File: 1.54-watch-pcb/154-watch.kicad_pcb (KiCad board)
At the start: 4 copper layers, 50.3 x 33 mm, 59 parts, among them J1 CONN_AFC24-S24FIC-00_JUS, J2 Conn_01x06_Female, J3 USB_C_Programming, J4 Jack-DC, J5 Conn_01x02_Male, Q1 Si1308, Q2 BC817, Q3 BC817, Q4 Si2301CDS, SW1 RESET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

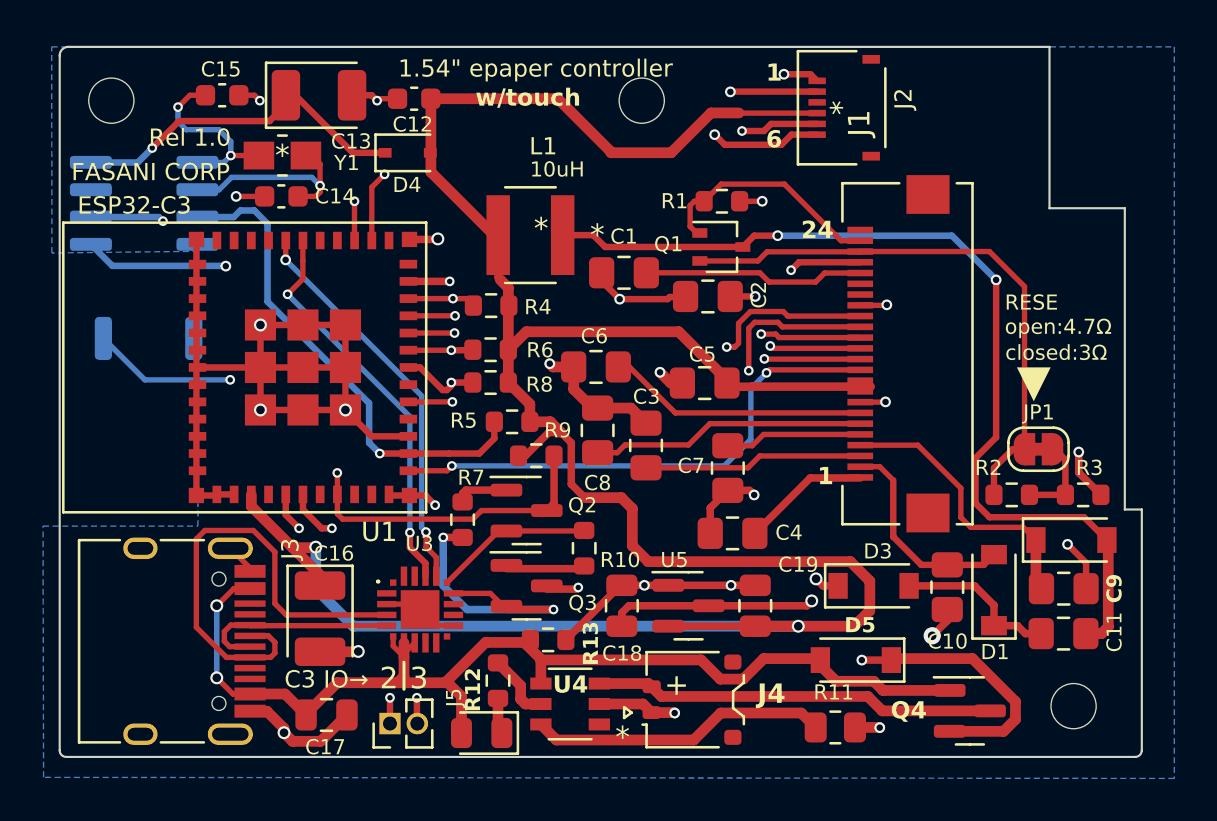
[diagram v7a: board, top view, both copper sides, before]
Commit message: 1.54 turn U2 RTC to backCU
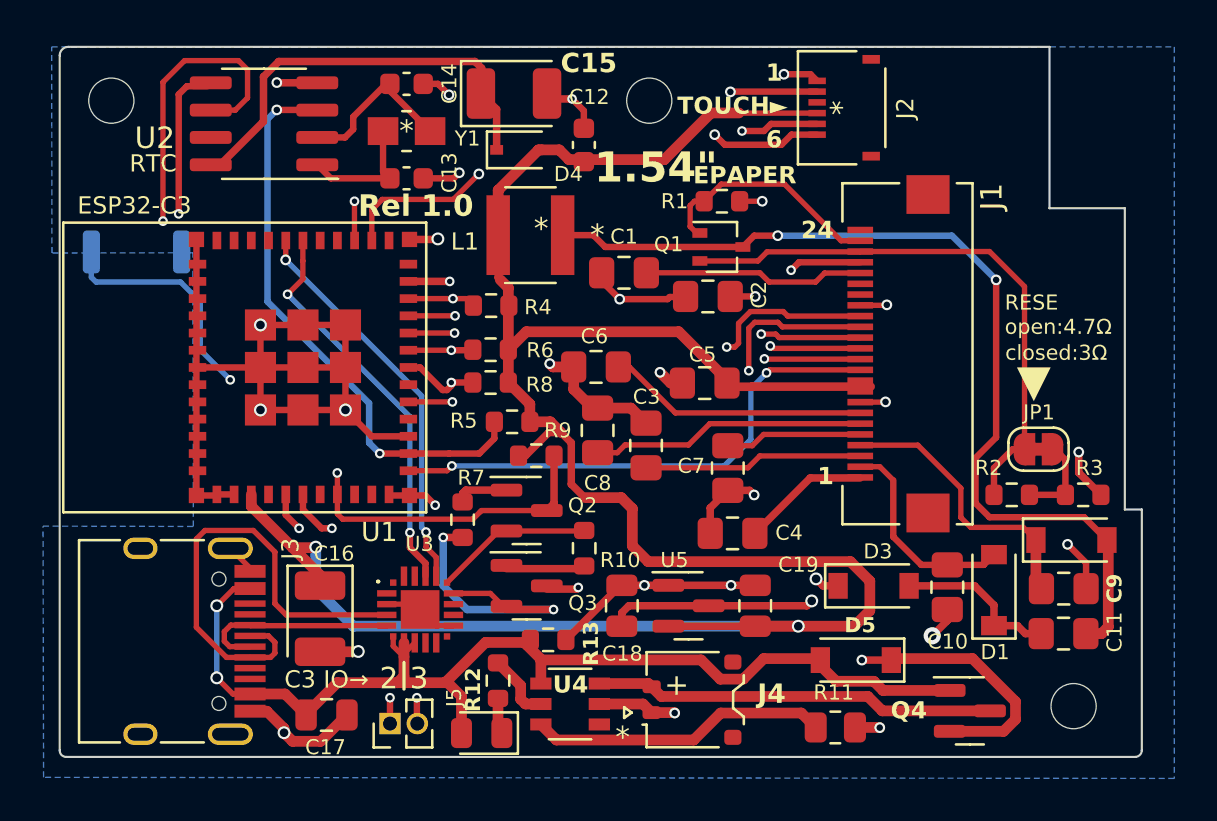
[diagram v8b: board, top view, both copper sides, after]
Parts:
- U2: moved to F.Cu
- moved C13 9.40 mm to (88.1, 35.6)
- moved C15 9.06 mm to (93.1, 31.7)
- moved C12 8.17 mm to (96.4, 34.1), turned to -90 degrees
- moved C14 7.82 mm to (88.1, 31.2), turned to 180 degrees
- moved U2 6.69 mm to (81.5, 33.1)
- moved Y1 5.88 mm to (88.1, 33.4)
- moved D4 5.18 mm to (93.4, 34.3)
- moved SW1 4.06 mm to (75.6, 39.0)
- moved H3 0.35 mm to (99.4, 32.0)
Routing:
- net /I2C_SCL: track 47.7 -> 58.6 mm
- net +3V3: track 121.1 -> 112.3 mm
- net Net-(Q2-C): track 29.5 -> 33.7 mm
- net Net-(#FLG01-pwr): track 16.3 -> 20.0 mm, vias 1 -> 0
- net /RTC_INT: track 22.9 -> 26.6 mm, vias 1 -> 2
- net /I2C_SDA: track 45.4 -> 49.0 mm
- net GND: track 100.2 -> 103.1 mm, vias 26 -> 27
- net Net-(U2-OSCI): track 8.65 -> 5.96 mm, vias 2 -> 0
- net Net-(U2-OSCO): track 9.33 -> 7.71 mm, vias 1 -> 0
- net /EPD_DC: track 28.6 -> 28.0 mm
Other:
- board text added: "1.54{dblquote}"
- board text added: "200x200 PCF8563 RTC. I2C GPIOs: RTC_INT=1 | SDA=5 SCL=4 TOUCH_INT=8 (IO w/pullup) SPI GPIOs: MOSI=0 CLK=6 CS=19 RST=10 BUSY=7 DC=18"
- board text added: "EPAPER"
- board text added: "OPEN SOURCE PCB"
- board text added: "TOUCH►"
- board text added: "►"
- board text removed: "1.54{dblquote} epaper controller"
- board text removed: "200x200 PCF8563 RTC. I2C GPIOs: RTC_INT=2 | SDA=5 SCL=4 SPI GPIOs: MOSI=0 CLK=6 CS=19 RST=10 BUSY=7 DC=18"
- board text removed: "3 RST 4 VDD 5 SCL 6 SDA"
- board text removed: "FASANI CORP"
- board text removed: "TOUCH Pinup: 1 GND 2 INT"
- board text removed: "w/touch"
